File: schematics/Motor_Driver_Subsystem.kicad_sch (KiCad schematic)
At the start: 0 parts

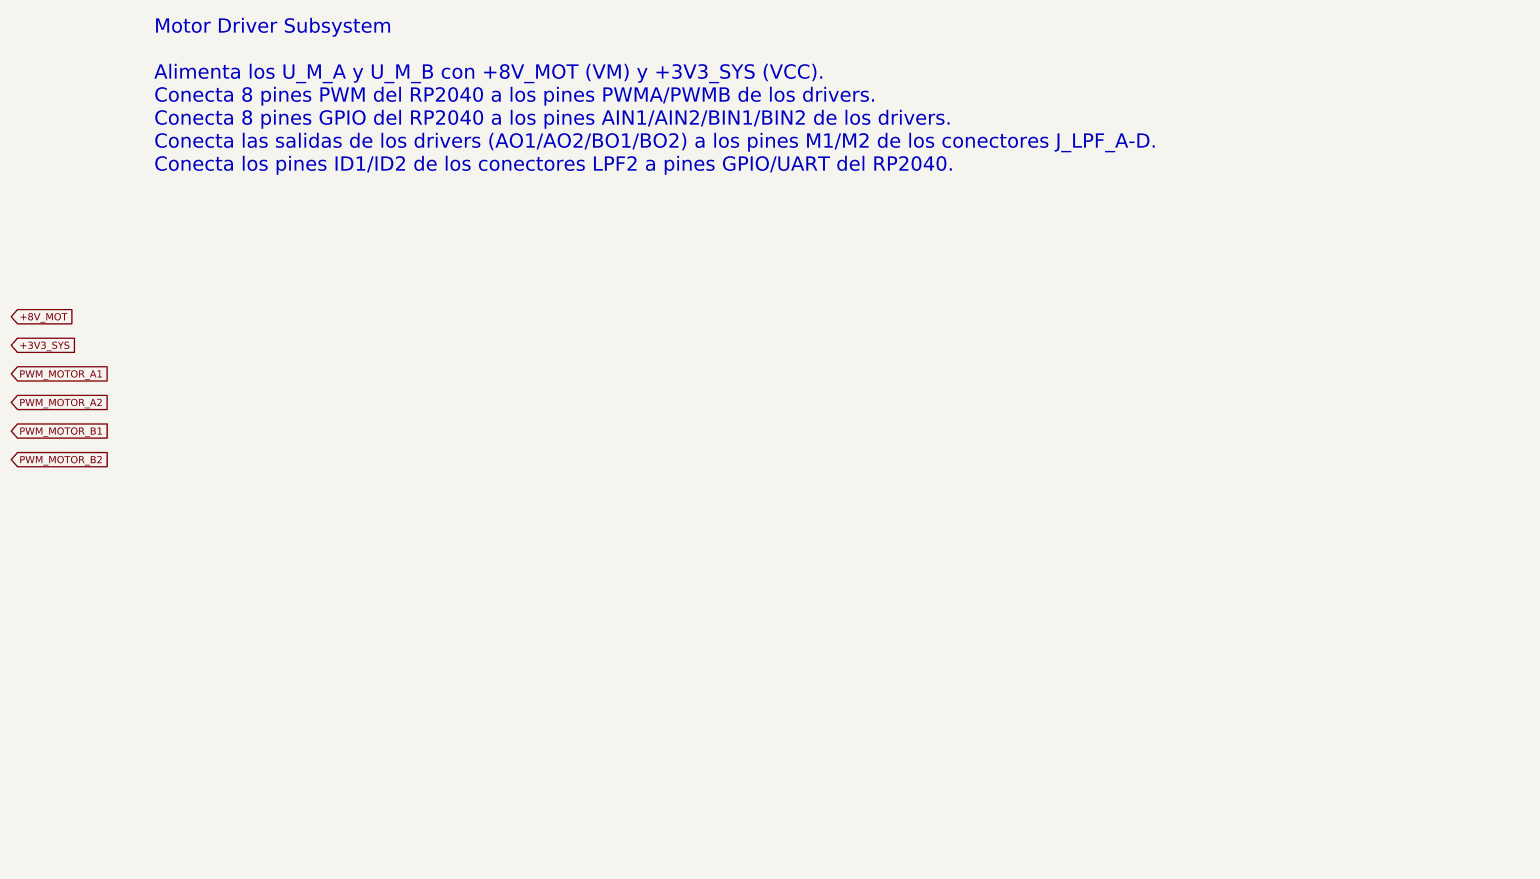
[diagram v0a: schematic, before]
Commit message: Añadir esquemático detallado del subsistema de drivers de motor
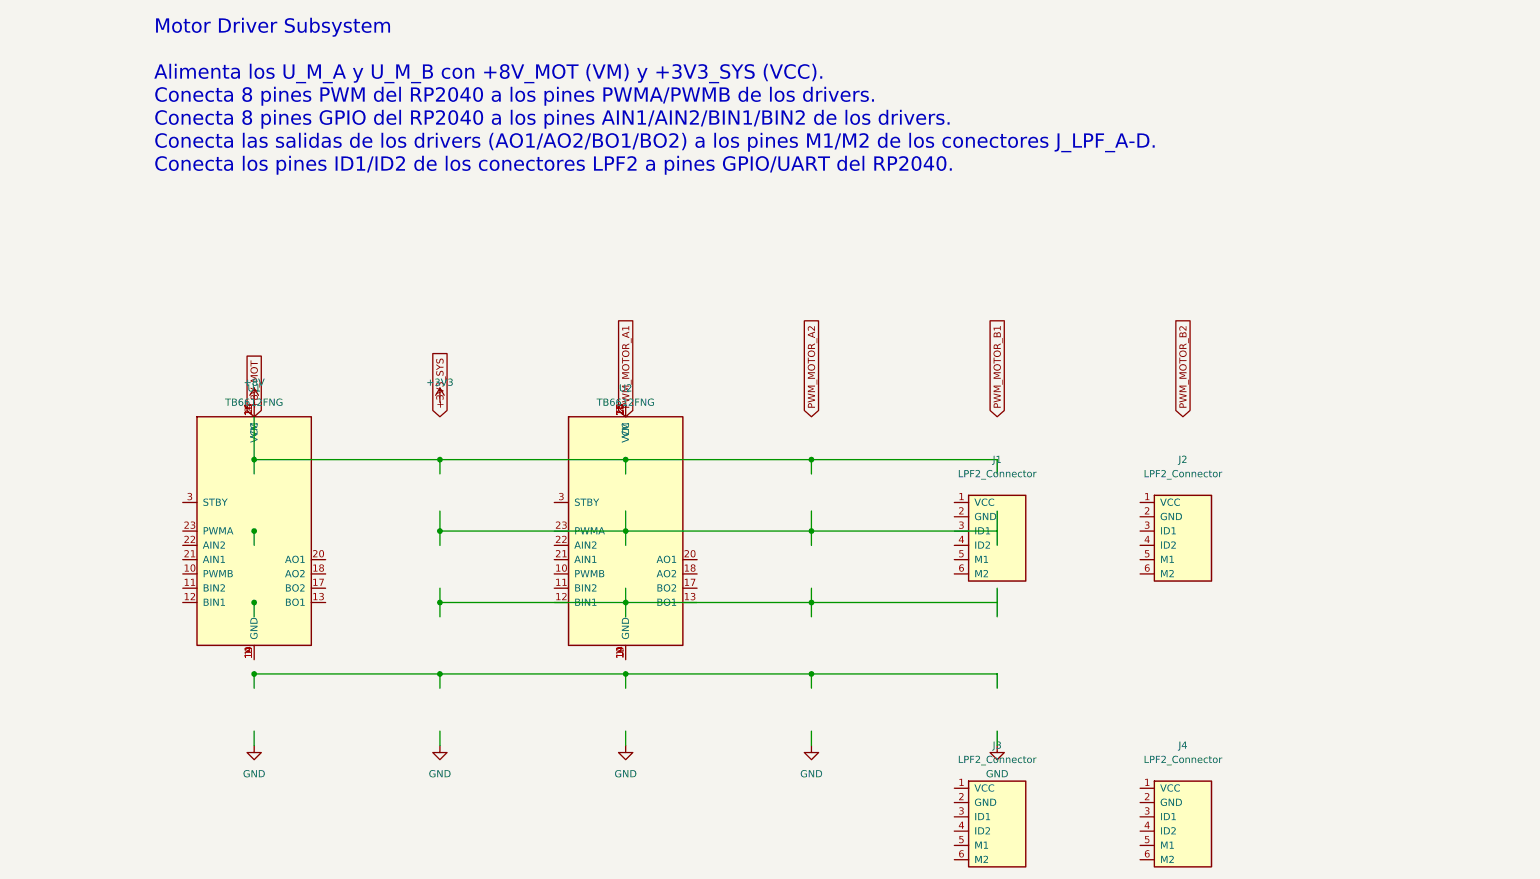
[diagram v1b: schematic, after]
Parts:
- added J1, J2, J3, J4: LPF2_Connector, Custom:LPF2_Connector, symbol custom_symbols:LPF2_Connector
- added U1, U2: TB6612FNG, Package_SO:SSOP-24_5.3x8.2mm_P0.65mm, symbol Driver_Motor:TB6612FNG
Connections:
- new net: U1.1 (GND), U1.14 (GND), U1.19 (GND)
- new net: U2.1 (GND), U2.14 (GND), U2.19 (GND)
- new net: U2.15 (VM), U2.16 (VM), U2.2 (VCC), U2.24 (VM)
- new net +8V: U1.15 (VM), U1.16 (VM), U1.2 (VCC), U1.24 (VM)
